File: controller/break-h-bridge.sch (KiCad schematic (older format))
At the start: 33 parts, among them J24 CONN_01X02, J5 CONN_01X02, Q7 Q_NMOS_GSD, U7 SN74AHCT1G14DBVR, U8 VNH3SP30

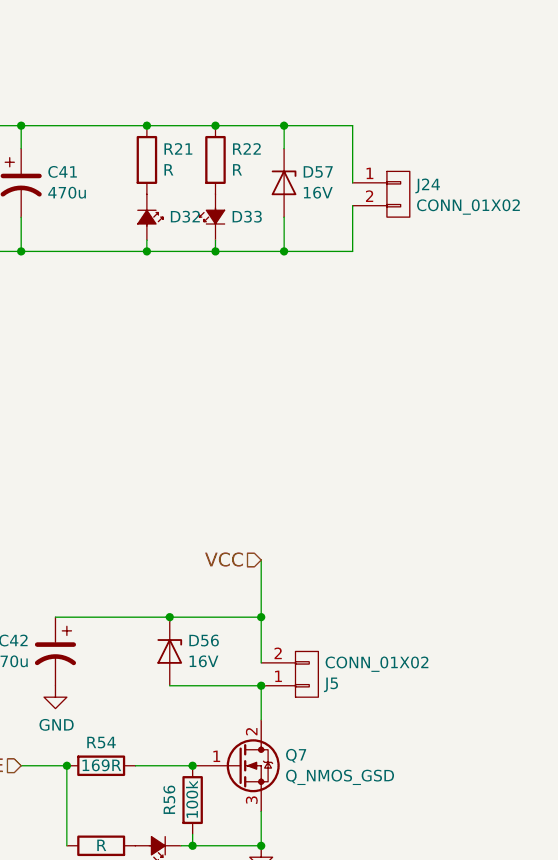
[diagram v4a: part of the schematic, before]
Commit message: Update the 5 and 2 pin terminal footprints, shuffle around some tracks
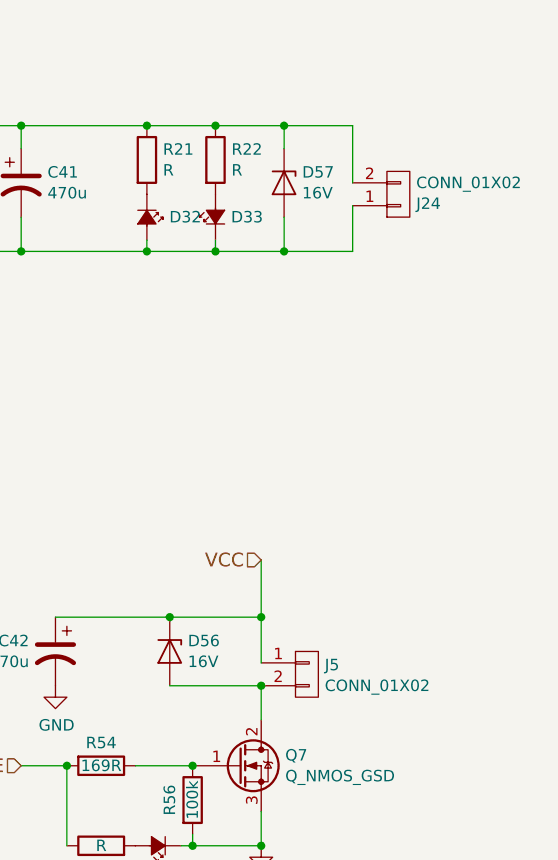
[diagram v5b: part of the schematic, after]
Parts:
- J24, J5: footprint Connectors_Terminal_Blocks:TerminalBlock_Pheonix_MKDS1.5-2pol -> smalsiukas-footpints:TerminalBlock_5.08-2pol
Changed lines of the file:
@@
 F 0 "J24" H 9128 2741 50  0000 L CNN
 F 1 "CONN_01X02" H 9128 2650 50  0000 L CNN
-F 2 "Connectors_Terminal_Blocks:TerminalBlock_Pheonix_MKDS1.5-2pol" H -150 -1250 50  0001 C CNN
+F 2 "smalsiukas-footpints:TerminalBlock_5.08-2pol" H -150 -1250 50  0001 C CNN
 F 3 "" H -150 -1250 50  0001 C CNN
 F 4 "?" H 9050 2700 60  0001 C CNN "PartNo"
@@
 F 6 "?" H 9050 2700 60  0001 C CNN "Distributor"
 	1    9050 2700
-	1    0    0    -1
+	1    0    0    1
 $EndComp
 Wire Wire Line
@@
 F 0 "J5" H 8728 4841 50  0000 L CNN
 F 1 "CONN_01X02" H 8728 4750 50  0000 L CNN
-F 2 "Connectors_Terminal_Blocks:TerminalBlock_Pheonix_MKDS1.5-2pol" H -550 850 50  0001 C CNN
+F 2 "smalsiukas-footpints:TerminalBlock_5.08-2pol" H -550 850 50  0001 C CNN
 F 3 "" H -550 850 50  0001 C CNN
 F 4 "?" H 8650 4800 60  0001 C CNN "PartNo"
@@
 F 6 "?" H 8650 4800 60  0001 C CNN "Distributor"
 	1    8650 4800
-	1    0    0    1
+	1    0    0    -1
 $EndComp
 Text HLabel 8450 4300 0    60   Input ~ 0

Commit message: Various fixes and comments to the controller board, also making it suitable for non-plated holes.
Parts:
- U7: Distributor 1105925 -> 1470878; PartNo SN74AHCT1G14DBVR -> SN74LVC1G14DBVR
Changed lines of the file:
@@
 encoding utf-8
 Sheet 8 10
-Title ""
-Date ""
-Rev ""
-Comp ""
-Comment1 ""
+Title "Smalsiukas - Toyota lifter hack"
+Date "2017-04-01"
+Rev "Rev1"
+Comp "TECHNARIUM"
+Comment1 "Albertas Mickėnas"
 Comment2 ""
 Comment3 ""
@@
 F 2 "TO_SOT_Packages_SMD:SOT-23-5_HandSoldering" H -350 -1300 50  0001 C CNN
 F 3 "" H -350 -1300 50  0001 C CNN
-F 4 "SN74AHCT1G14DBVR" H 4800 1500 60  0001 C CNN "PartNo"
+F 4 "SN74LVC1G14DBVR" H 4800 1500 60  0001 C CNN "PartNo"
 F 5 "TEXAS INSTRUMENTS" H 4800 1500 60  0001 C CNN "Manufacturer"
-F 6 "1105925" H 4800 1500 60  0001 C CNN "Distributor"
+F 6 "1470878" H 4800 1500 60  0001 C CNN "Distributor"
 	1    4800 1500
 	1    0    0    -1
